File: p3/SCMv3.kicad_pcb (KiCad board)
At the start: 2 copper layers, 58.7 x 110.9 mm, 127 parts, among them IC1 40106, IC2 40106, IC3 TL082, J1 Conn_01x06, J1-OUT8 JACK-MONO-SWB, J2 Conn_01x02, J2-OUT7 JACK-MONO-SWB, J3 POWER, J3-OUT6 JACK-MONO-SWB, J4 Conn_01x02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

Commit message: Revert "Merge remote-tracking branch 'origin/main' into main"
This reverts commit 63f0bb0c0b25969e804c40226811b6ef72d39a13.
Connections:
- U1 pad 22: /UC_CLK_IN -> /SWDIO
- U1 pad 23: /SWDIO -> /SWCLK
- U1 pad 24: /SWCLK -> /UC_CLK_IN
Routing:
- net /UC_CLK_IN: track 87.6 -> 85.6 mm, vias 6 -> 4
- net /SWDIO: track 24.2 -> 25.1 mm

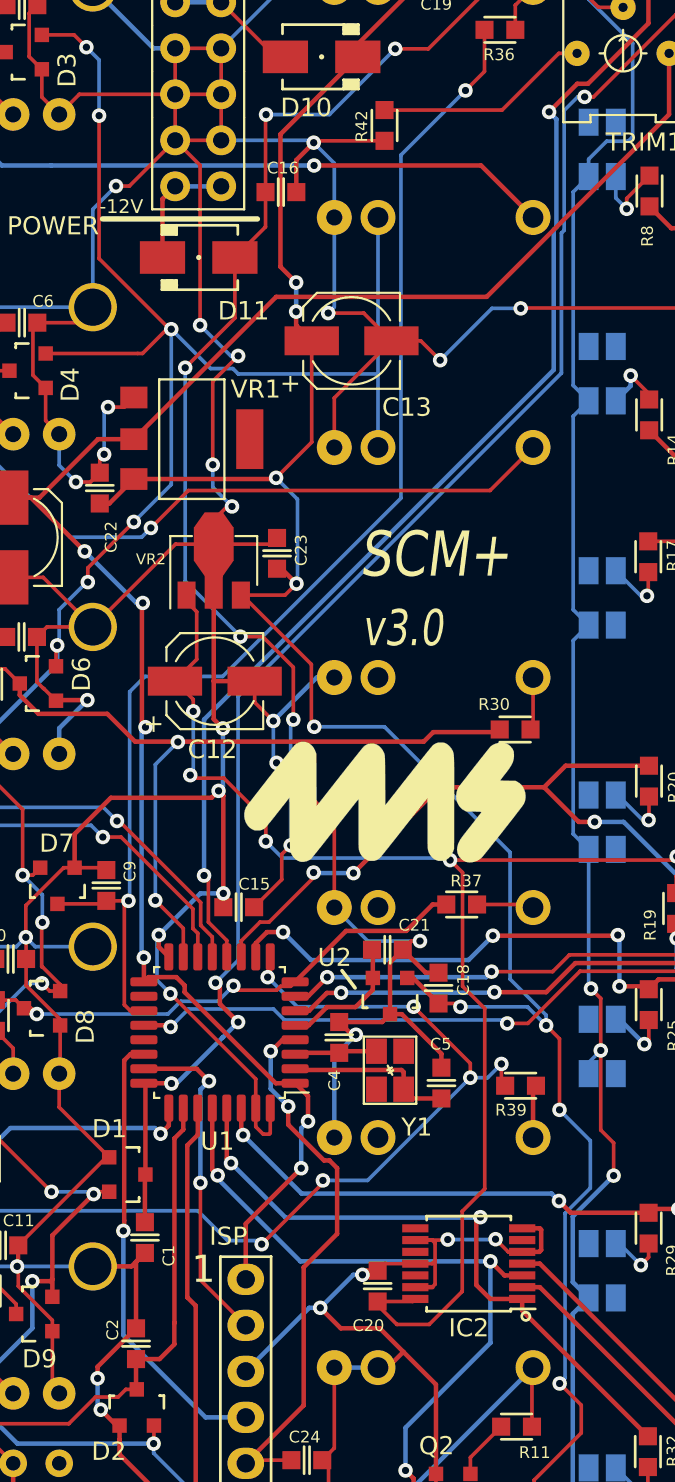
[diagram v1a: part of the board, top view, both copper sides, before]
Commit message: fixed routing error
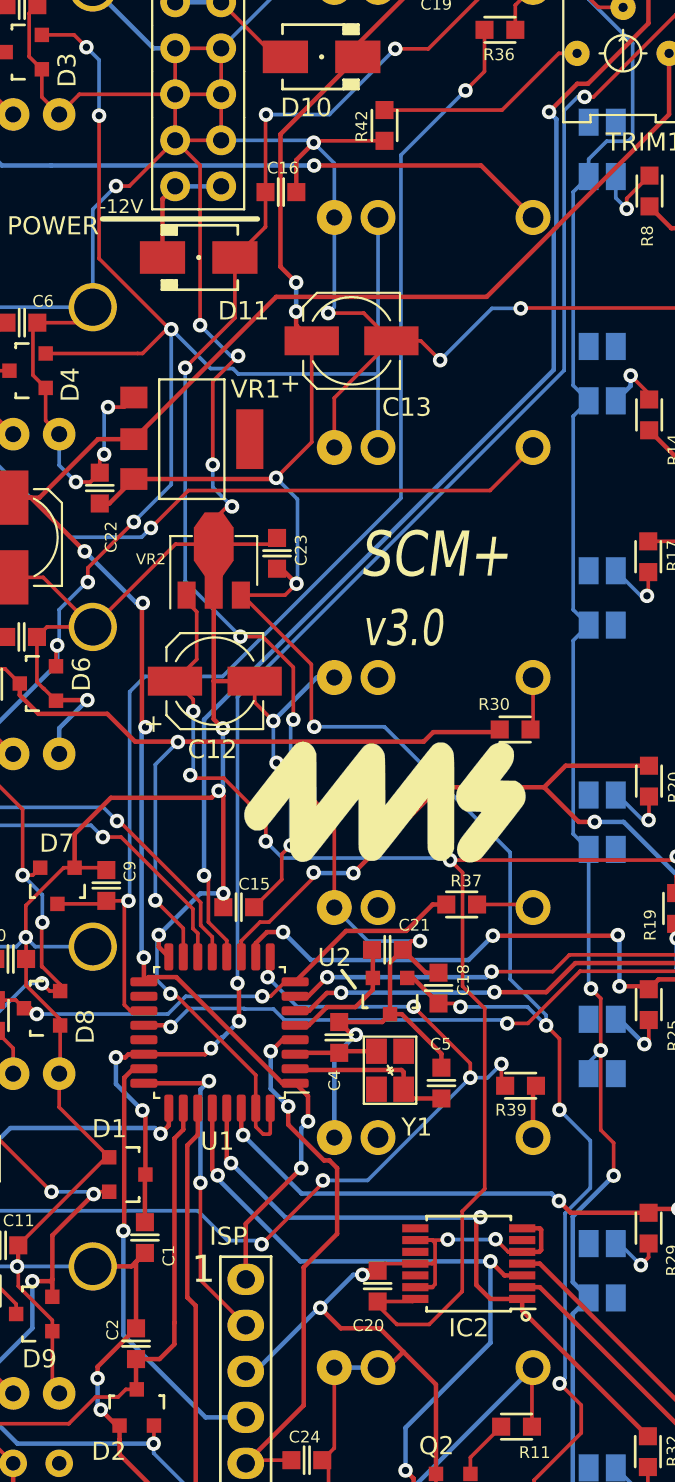
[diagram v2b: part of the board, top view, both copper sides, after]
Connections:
- U1 pad 22: /SWDIO -> /UC_CLK_IN
- U1 pad 23: /SWCLK -> /SWDIO
- U1 pad 24: /UC_CLK_IN -> /SWCLK
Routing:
- net /UC_CLK_IN: track 85.6 -> 87.6 mm, vias 4 -> 6
- net /SWDIO: track 25.1 -> 24.2 mm
